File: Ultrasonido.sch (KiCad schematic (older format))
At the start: 1 part, among them P4 CONN_01X04

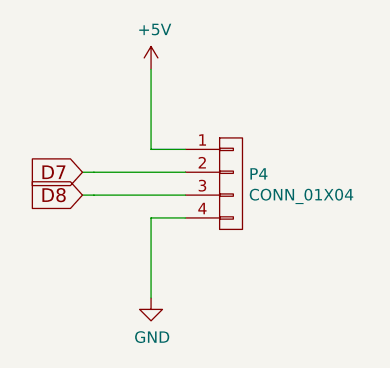
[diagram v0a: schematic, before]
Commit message: añaadido zocalo para sensor de temperatura y primera distribucion sobre la PCB
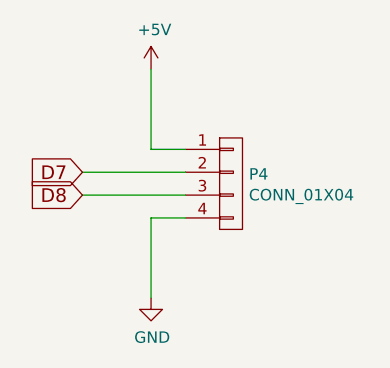
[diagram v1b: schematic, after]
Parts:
- P4: footprint (none) -> Socket_Strips:Socket_Strip_Straight_1x04
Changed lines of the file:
@@
 $Descr User 8268 5846
 encoding utf-8
-Sheet 11 13
+Sheet 11 14
 Title ""
 Date ""
@@
 F 0 "P4" H 3628 2341 50  0000 L CNN
 F 1 "CONN_01X04" H 3628 2250 50  0000 L CNN
-F 2 "" H 3550 2300 50  0000 C CNN
+F 2 "Socket_Strips:Socket_Strip_Straight_1x04" H 3550 2300 50  0001 C CNN
 F 3 "" H 3550 2300 50  0000 C CNN
 	1    3550 2300
@@
 	3200 2450 3200 2800
 $Comp
-L GND #PWR039
+L GND #PWR041
 U 1 1 57950B26
 P 3200 2800
-F 0 "#PWR039" H 3200 2550 50  0001 C CNN
+F 0 "#PWR041" H 3200 2550 50  0001 C CNN
 F 1 "GND" H 3205 2627 50  0000 C CNN
 F 2 "" H 3200 2800 50  0000 C CNN
@@
 	3200 2150 3200 1800
 $Comp
-L +5V #PWR040
+L +5V #PWR042
 U 1 1 57950B43
 P 3200 1800
-F 0 "#PWR040" H 3200 1650 50  0001 C CNN
+F 0 "#PWR042" H 3200 1650 50  0001 C CNN
 F 1 "+5V" H 3215 1973 50  0000 C CNN
 F 2 "" H 3200 1800 50  0000 C CNN
@@
 $EndComp
 Wire Wire Line
-	3350 2250 2950 2250
+	2900 2250 3350 2250
 Wire Wire Line
-	2950 2350 3350 2350
+	2900 2350 3350 2350
 Text GLabel 2900 2250 0    60   Input ~ 0
 D7
@@
 D8
 Wire Wire Line
-	2900 2250 2950 2250
-Wire Wire Line
 	2950 2250 2950 2250
-Wire Wire Line
-	2950 2350 2950 2350
-Wire Wire Line
-	2950 2350 2900 2350
 $Bitmap
 Pos 5200 2350

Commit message: finalizado enrutado provisional
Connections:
- net D7: now also P4.3 (P3); no longer P4.2 (P2)
- net D8: now also P4.2 (P2); no longer P4.3 (P3)
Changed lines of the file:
@@
 $Descr User 8268 5846
 encoding utf-8
-Sheet 11 14
+Sheet 11 15
 Title ""
 Date ""
@@
 	3200 2450 3200 2800
 $Comp
-L GND #PWR041
+L GND #PWR034
 U 1 1 57950B26
 P 3200 2800
-F 0 "#PWR041" H 3200 2550 50  0001 C CNN
+F 0 "#PWR034" H 3200 2550 50  0001 C CNN
 F 1 "GND" H 3205 2627 50  0000 C CNN
 F 2 "" H 3200 2800 50  0000 C CNN
@@
 	3200 2150 3200 1800
 $Comp
-L +5V #PWR042
+L +5V #PWR035
 U 1 1 57950B43
 P 3200 1800
-F 0 "#PWR042" H 3200 1650 50  0001 C CNN
+F 0 "#PWR035" H 3200 1650 50  0001 C CNN
 F 1 "+5V" H 3215 1973 50  0000 C CNN
 F 2 "" H 3200 1800 50  0000 C CNN
@@
 $EndComp
 Wire Wire Line
-	2900 2250 3350 2250
-Wire Wire Line
 	2900 2350 3350 2350
 Text GLabel 2900 2250 0    60   Input ~ 0
-D7
-Text GLabel 2900 2350 0    60   Input ~ 0
 D8
-Wire Wire Line
-	2950 2250 2950 2250
+Text GLabel 2900 2350 0    60   Input ~ 0
+D7
 $Bitmap
 Pos 5200 2350
@@
 EndData
 $EndBitmap
+Wire Wire Line
+	2900 2250 3350 2250
 $EndSCHEMATC

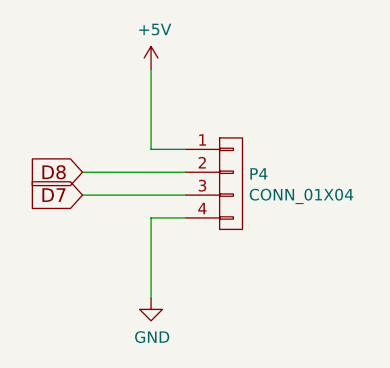
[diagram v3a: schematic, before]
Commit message: ordenar referencias de componentes
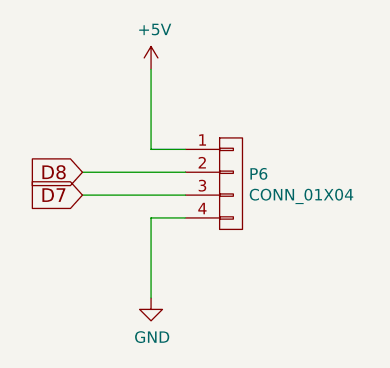
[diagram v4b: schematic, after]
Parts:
- P6: renamed from P4; Fabricante (none) -> NINIGI; Provedor (none) -> TME; Ref (none) -> ZL262-40SG; Ref_Proveedor (none) -> ZL262-40SG
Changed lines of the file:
@@
 $Descr User 8268 5846
 encoding utf-8
-Sheet 11 15
+Sheet 9 15
 Title ""
 Date ""
@@
 $EndDescr
 $Comp
-L CONN_01X04 P4
+L CONN_01X04 P6
 U 1 1 57950AD5
 P 3550 2300
-F 0 "P4" H 3628 2341 50  0000 L CNN
+F 0 "P6" H 3628 2341 50  0000 L CNN
 F 1 "CONN_01X04" H 3628 2250 50  0000 L CNN
 F 2 "Socket_Strips:Socket_Strip_Straight_1x04" H 3550 2300 50  0001 C CNN
 F 3 "" H 3550 2300 50  0000 C CNN
+F 4 "NINIGI" H 3550 2300 60  0001 C CNN "Fabricante"
+F 5 "ZL262-40SG" H 3550 2300 60  0001 C CNN "Ref"
+F 6 "~" H 3550 2300 60  0001 C CNN "Potencia"
+F 7 "~" H 3550 2300 60  0001 C CNN "Tolerancia"
+F 8 "TME" H 3550 2300 60  0001 C CNN "Provedor"
+F 9 "ZL262-40SG" H 3550 2300 60  0001 C CNN "Ref_Proveedor"
 	1    3550 2300
 	1    0    0    -1
@@
 	3200 2450 3200 2800
 $Comp
-L GND #PWR034
+L GND #PWR25
 U 1 1 57950B26
 P 3200 2800
-F 0 "#PWR034" H 3200 2550 50  0001 C CNN
+F 0 "#PWR25" H 3200 2550 50  0001 C CNN
 F 1 "GND" H 3205 2627 50  0000 C CNN
 F 2 "" H 3200 2800 50  0000 C CNN
@@
 	3200 2150 3200 1800
 $Comp
-L +5V #PWR035
+L +5V #PWR24
 U 1 1 57950B43
 P 3200 1800
-F 0 "#PWR035" H 3200 1650 50  0001 C CNN
+F 0 "#PWR24" H 3200 1650 50  0001 C CNN
 F 1 "+5V" H 3215 1973 50  0000 C CNN
 F 2 "" H 3200 1800 50  0000 C CNN

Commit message: añadidos driver para led y conectores para fotodiodos infrarrojos
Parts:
- P10: renamed from P6; Ref ZL262-40SG -> ZL262-4SG; Ref_Proveedor ZL262-40SG -> ZL262-4SG
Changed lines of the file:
@@
 EESchema Schematic File Version 2
+LIBS:Interfaces
+LIBS:Nano_PB-rescue
 LIBS:Sensores
 LIBS:power
@@
 LIBS:valves
 LIBS:MyLibrary
+LIBS:matriz_led
 LIBS:Nano_PB-cache
-EELAYER 25 0
+EELAYER 26 0
 EELAYER END
 $Descr User 8268 5846
 encoding utf-8
-Sheet 9 15
+Sheet 9 16
 Title "Puerto de expansión para sensor por ultrasonidos"
-Date "2016-08-07"
-Rev "V.0.2"
+Date "2017-01-04"
+Rev "V.0.3"
 Comp "NanoPlayBoard"
 Comment1 "Creada por Antonio Morales"
@@
 $EndDescr
 $Comp
-L CONN_01X04 P6
+L CONN_01X04 P10
 U 1 1 57950AD5
 P 3550 2300
-F 0 "P6" H 3628 2341 50  0000 L CNN
+F 0 "P10" H 3628 2341 50  0000 L CNN
 F 1 "CONN_01X04" H 3628 2250 50  0000 L CNN
 F 2 "Socket_Strips:Socket_Strip_Straight_1x04" H 3550 2300 50  0001 C CNN
 F 3 "" H 3550 2300 50  0000 C CNN
 F 4 "NINIGI" H 3550 2300 60  0001 C CNN "Fabricante"
-F 5 "ZL262-40SG" H 3550 2300 60  0001 C CNN "Ref"
+F 5 "ZL262-4SG" H 3550 2300 60  0001 C CNN "Ref"
 F 6 "~" H 3550 2300 60  0001 C CNN "Potencia"
 F 7 "~" H 3550 2300 60  0001 C CNN "Tolerancia"
 F 8 "TME" H 3550 2300 60  0001 C CNN "Provedor"
-F 9 "ZL262-40SG" H 3550 2300 60  0001 C CNN "Ref_Proveedor"
+F 9 "ZL262-4SG" H 3550 2300 60  0001 C CNN "Ref_Proveedor"
 	1    3550 2300
 	1    0    0    -1
@@
 	3200 2450 3200 2800
 $Comp
-L GND #PWR026
+L GND #PWR047
 U 1 1 57950B26
 P 3200 2800
-F 0 "#PWR026" H 3200 2550 50  0001 C CNN
+F 0 "#PWR047" H 3200 2550 50  0001 C CNN
 F 1 "GND" H 3205 2627 50  0000 C CNN
 F 2 "" H 3200 2800 50  0000 C CNN
@@
 	3200 2150 3200 1800
 $Comp
-L +5V #PWR027
+L +5V #PWR048
 U 1 1 57950B43
 P 3200 1800
-F 0 "#PWR027" H 3200 1650 50  0001 C CNN
+F 0 "#PWR048" H 3200 1650 50  0001 C CNN
 F 1 "+5V" H 3215 1973 50  0000 C CNN
 F 2 "" H 3200 1800 50  0000 C CNN
@@
 06 02 60 F6 9F DA 42 B0 B0 55 7C 82 77 03 68 E5 1B 12 C1 B5 DD C9 FA 1E 7B D0 9D 1E 05 40 9E BA
 98 9D D6 04 BC A7 2E 26 EC 4A F4 BB 3F E8 CE 7F 77 FC 6E 1E 01 69 4E 96 BA 18 AA 4C FF 48 93 C5
-00 79 B2 18 20 6F 00 4A 5F 07 5A 8D 19 83 DE 00 00 00 00 49 45 4E 44 AE 42 60 82 00
+00 79 B2 18 20 6F 00 4A 5F 07 5A 8D 19 83 DE 00 00 00 00 49 45 4E 44 AE 42 60 82
 EndData
 $EndBitmap
@@
 50 17 92 01 51 92 64 0C CE 27 7B 4E 87 A3 FC C9 E9 39 BC D0 3B DC 1F CF E6 3C 60 30 83 10 3D 18
 F4 0B 89 52 73 00 8B 80 91 08 28 22 8F 6D AB AA BD D3 E7 C4 3E A7 59 B4 A9 94 4D 1C A1 84 52 AC
-9A 46 F6 7A E1 FF 00 F0 A4 0C 74 26 CB 7B D1 00 00 00 00 49 45 4E 44 AE 42 60 82 00
+9A 46 F6 7A E1 FF 00 F0 A4 0C 74 26 CB 7B D1 00 00 00 00 49 45 4E 44 AE 42 60 82
 EndData
 $EndBitmap
